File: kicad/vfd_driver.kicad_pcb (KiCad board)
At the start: 2 copper layers, 181.6 x 35.3 mm, 48 parts, among them CON1 AVR-ISP-6, J1 PWR, J2 Display, J6 MH, J7 MH, J8 MH, J9 MH, U1 ATTINY2313-20SU, U10 74HC595, U11 74HC595, U12 74HC595, U13 74HC595, U14 ULN2803A, U15 ULN2803A, U16 ULN2003, U17 ULN2003, U18 LM1117-3.3, U19 LT1073, U2 74HC595, U3 74HC595, U4 74HC595, U5 74HC595, U6 ULN2803A, U7 ULN2003, U8 ULN2003, U9 ULN2003

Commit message: routing
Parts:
- removed J8, J9: MH, Mounting_Holes:MountingHole_3.2mm_M3_DIN965_Pad
- removed U1: ATTINY2313-20SU, Housings_SOIC:SOIC-20W_7.5x12.8mm_Pitch1.27mm
- removed U2, U3, U4: 74HC595, Housings_SOIC:SOIC-16_3.9x9.9mm_Pitch1.27mm
- added J3: MH, Mounting_Holes:MountingHole_3.2mm_M3_DIN965_Pad, F.Cu at (19.1, 49.5)
- added J4: MH, Mounting_Holes:MountingHole_3.2mm_M3_DIN965_Pad, F.Cu at (19.1, 17.8)
- added J5: MH, Mounting_Holes:MountingHole_3.2mm_M3_DIN965_Pad, F.Cu at (191.8, 17.8)
- added R16: 1k, Resistors_SMD:R_0805_HandSoldering, B.Cu at (55.4, 16.8)
- added R17: 1k, Resistors_SMD:R_0805_HandSoldering, B.Cu at (57.4, 16.8)
- added R18: 1k, Resistors_SMD:R_0805_HandSoldering, B.Cu at (59.4, 16.8)
- added R19: 1k, Resistors_SMD:R_0805_HandSoldering, B.Cu at (61.5, 16.8)
- added R20: 1k, Resistors_SMD:R_0805_HandSoldering, B.Cu at (63.5, 16.8)
- added R21: 1k, Resistors_SMD:R_0805_HandSoldering, B.Cu at (65.5, 16.8)
- added R22: 1k, Resistors_SMD:R_0805_HandSoldering, B.Cu at (67.6, 16.8)
- added R23: 1k, Resistors_SMD:R_0805_HandSoldering, B.Cu at (69.6, 16.8)
- added R24: 1k, Resistors_SMD:R_0805_HandSoldering, B.Cu at (71.6, 16.8)
- added R25: 1k, Resistors_SMD:R_0805_HandSoldering, B.Cu at (73.7, 16.8)
- added R26: 1k, Resistors_SMD:R_0805_HandSoldering, B.Cu at (75.7, 16.8)
- added R27: 1k, Resistors_SMD:R_0805_HandSoldering, B.Cu at (77.7, 16.8)
- added R28: 1k, Resistors_SMD:R_0805_HandSoldering, B.Cu at (79.8, 16.8)
- added R29: 1k, Resistors_SMD:R_0805_HandSoldering, B.Cu at (81.8, 16.8)
- added R30: 1k, Resistors_SMD:R_0805_HandSoldering, B.Cu at (83.8, 16.8)
- added R31: 1k, Resistors_SMD:R_0805_HandSoldering, B.Cu at (85.9, 16.8)
- added R32: 1k, Resistors_SMD:R_0805_HandSoldering, B.Cu at (87.9, 16.8)
- added R33: 1k, Resistors_SMD:R_0805_HandSoldering, B.Cu at (89.9, 16.8)
- added R34: 1k, Resistors_SMD:R_0805_HandSoldering, B.Cu at (91.9, 16.8)
- added R35: 1k, Resistors_SMD:R_0805_HandSoldering, B.Cu at (94.0, 16.8)
- added R36: 1k, Resistors_SMD:R_0805_HandSoldering, B.Cu at (96.0, 16.8)
- added R37: 1k, Resistors_SMD:R_0805_HandSoldering, B.Cu at (98.0, 16.8)
- added R38: 1k, Resistors_SMD:R_0805_HandSoldering, B.Cu at (100.1, 16.8)
- added R39: 1k, Resistors_SMD:R_0805_HandSoldering, B.Cu at (102.1, 16.8)
- added R40: 1k, Resistors_SMD:R_0805_HandSoldering, B.Cu at (104.1, 16.8)
- added R41: 1k, Resistors_SMD:R_0805_HandSoldering, B.Cu at (106.2, 16.8)
- added R42: 1k, Resistors_SMD:R_0805_HandSoldering, B.Cu at (108.2, 16.8)
- added R43: 1k, Resistors_SMD:R_0805_HandSoldering, B.Cu at (110.2, 16.8)
- added R44: 1k, Resistors_SMD:R_0805_HandSoldering, B.Cu at (112.3, 16.8)
- added R45: 1k, Resistors_SMD:R_0805_HandSoldering, B.Cu at (114.3, 16.8)
- added R46: 1k, Resistors_SMD:R_0805_HandSoldering, B.Cu at (116.3, 16.8)
- added R47: 1k, Resistors_SMD:R_0805_HandSoldering, B.Cu at (118.4, 16.8)
- added R48: 1k, Resistors_SMD:R_0805_HandSoldering, B.Cu at (120.4, 16.8)
- added R49: 1k, Resistors_SMD:R_0805_HandSoldering, B.Cu at (122.4, 16.8)
- added R50: 1k, Resistors_SMD:R_0805_HandSoldering, B.Cu at (124.5, 16.8)
- added R51: 1k, Resistors_SMD:R_0805_HandSoldering, B.Cu at (126.5, 16.8)
- added R52: 1k, Resistors_SMD:R_0805_HandSoldering, B.Cu at (128.5, 16.8)
- added R53: 1k, Resistors_SMD:R_0805_HandSoldering, B.Cu at (130.6, 16.8)
- added R54: 1k, Resistors_SMD:R_0805_HandSoldering, B.Cu at (132.6, 16.8)
- added R55: 1k, Resistors_SMD:R_0805_HandSoldering, B.Cu at (134.6, 16.8)
- added R56: 1k, Resistors_SMD:R_0805_HandSoldering, B.Cu at (136.7, 16.8)
- added R57: 1k, Resistors_SMD:R_0805_HandSoldering, B.Cu at (138.7, 16.8)
- added R58: 1k, Resistors_SMD:R_0805_HandSoldering, B.Cu at (140.7, 16.8)
- added R59: 1k, Resistors_SMD:R_0805_HandSoldering, B.Cu at (142.7, 16.8)
- added R6: 1M, Resistors_SMD:R_1206, B.Cu at (183.6, 40.4)
- added R60: 1k, Resistors_SMD:R_0805_HandSoldering, B.Cu at (144.8, 16.8)
- added R61: 1k, Resistors_SMD:R_0805_HandSoldering, B.Cu at (146.8, 16.8)
- added R62: 1k, Resistors_SMD:R_0805_HandSoldering, B.Cu at (148.8, 16.8)
- added R63: 1k, Resistors_SMD:R_0805_HandSoldering, B.Cu at (150.9, 16.8)
- added R64: 1k, Resistors_SMD:R_0805_HandSoldering, B.Cu at (152.9, 16.8)
- added R65: 1k, Resistors_SMD:R_0805_HandSoldering, B.Cu at (154.9, 16.8)
- added R66: 1k, Resistors_SMD:R_0805_HandSoldering, B.Cu at (157.0, 16.8)
- added R67: 1k, Resistors_SMD:R_0805_HandSoldering, B.Cu at (159.0, 16.8)
- added R68: 1k, Resistors_SMD:R_0805_HandSoldering, B.Cu at (161.0, 16.8)
- added R69: 1k, Resistors_SMD:R_0805_HandSoldering, B.Cu at (163.1, 16.8)
- added R7: 4k7, Resistors_SMD:R_1206, B.Cu at (183.6, 34.8)
- added R70: 1k, Resistors_SMD:R_0805_HandSoldering, B.Cu at (165.1, 16.8)
- added R71: 1k, Resistors_SMD:R_0805_HandSoldering, B.Cu at (167.1, 16.8)
- added R72: 1k, Resistors_SMD:R_0805_HandSoldering, B.Cu at (169.2, 16.8)
- added R73: 0, Resistors_SMD:R_1206, B.Cu at (65.5, 29.3)
- added R74: 0, Resistors_SMD:R_1206, B.Cu at (78.9, 29.3)
- added R75: 0, Resistors_SMD:R_1206, B.Cu at (93.1, 29.3)
- added R76: 0, Resistors_SMD:R_1206, B.Cu at (106.7, 29.3)
- added R77: 0, Resistors_SMD:R_1206, B.Cu at (120.9, 29.3)
- added R78: 0, Resistors_SMD:R_1206, B.Cu at (136.0, 30.2)
- added R79: 0, Resistors_SMD:R_1206, B.Cu at (152.0, 30.4)
- added R80: 0, Resistors_SMD:R_1206, B.Cu at (146.1, 50.4)
- added U20: 74HC595, Housings_SOIC:SOIC-16_3.9x9.9mm_Pitch1.27mm, B.Cu at (145.4, 43.2)
- added U21: ULN2803A, Housings_SOIC:SOIC-18W_7.5x11.6mm_Pitch1.27mm, B.Cu at (143.5, 30.5)
- added U22: 74HC595, Housings_SOIC:SOIC-16_3.9x9.9mm_Pitch1.27mm, B.Cu at (161.3, 43.2)
- added U23: ULN2803A, Housings_SOIC:SOIC-18W_7.5x11.6mm_Pitch1.27mm, B.Cu at (159.4, 30.5)
- C2: value 100n -> 47µ; footprint Capacitors_SMD:C_0805_HandSoldering -> Capacitors_THT:CP_Radial_Tantal_D4.5mm_P2.50mm
- C4: value 47µ -> 100n; footprint Capacitors_THT:CP_Radial_Tantal_D4.5mm_P2.50mm -> Capacitors_SMD:C_0805_HandSoldering; moved to B.Cu
- D1: value 1N5818 -> LED; footprint Diodes_SMD:D_SMA_Handsoldering -> LEDs:LED_0805
- D2: value LED -> 1N5818; footprint LEDs:LED_0805 -> Diodes_SMD:D_SMA_Handsoldering
- J2: value Display -> MH; footprint modules:vfd_FUTABA_24-SD-01GK_24x1 -> Mounting_Holes:MountingHole_3.2mm_M3_DIN965_Pad
- J6: value MH -> Display; footprint Mounting_Holes:MountingHole_3.2mm_M3_DIN965_Pad -> modules:vfd_FUTABA_24-SD-01GK_24x1
- J7: value MH -> Step; footprint Mounting_Holes:MountingHole_3.2mm_M3_DIN965_Pad -> Connectors:PINHEAD1-2
- R1: value 10k -> 1k; footprint Resistors_SMD:R_1206 -> Capacitors_SMD:C_0805_HandSoldering
- R2: value 100 -> 1k; footprint Resistors_SMD:R_1206 -> Capacitors_SMD:C_0805_HandSoldering
- R3: value 1M -> 10k
- R4: value 4k7 -> 470
- R5: value 470 -> 100
- U11, U13: value 74HC595 -> ULN2003
- U14: value ULN2803A -> 74HC595; footprint Housings_SOIC:SOIC-18W_7.5x11.6mm_Pitch1.27mm -> Housings_SOIC:SOIC-16_3.9x9.9mm_Pitch1.27mm
- U15: value ULN2803A -> ULN2003; footprint Housings_SOIC:SOIC-18W_7.5x11.6mm_Pitch1.27mm -> Housings_SOIC:SOIC-16_3.9x9.9mm_Pitch1.27mm
- U16, U8: value ULN2003 -> 74HC595
- U18: value LM1117-3.3 -> 74HC595; footprint modules:SOT-223_pin4_3 -> Housings_SOIC:SOIC-16_3.9x9.9mm_Pitch1.27mm
- U19: value LT1073 -> ULN2803A; footprint Housings_SOIC:SOIC-8_3.9x4.9mm_Pitch1.27mm -> Housings_SOIC:SOIC-18W_7.5x11.6mm_Pitch1.27mm
- U5: value 74HC595 -> LM1117-3.3; footprint Housings_SOIC:SOIC-16_3.9x9.9mm_Pitch1.27mm -> modules:SOT-223_pin4_3
- U6: value ULN2803A -> ATTINY2313-20SU; footprint Housings_SOIC:SOIC-18W_7.5x11.6mm_Pitch1.27mm -> Housings_SOIC:SOIC-20W_7.5x12.8mm_Pitch1.27mm
- U7: value ULN2003 -> LT1073; footprint Housings_SOIC:SOIC-16_3.9x9.9mm_Pitch1.27mm -> Housings_SOIC:SOIC-8_3.9x4.9mm_Pitch1.27mm
- moved R4 152.9 mm to (38.5, 49.9), turned to 270 degrees
- moved D2 151.8 mm to (177.3, 40.9)
- moved R3 148.3 mm to (42.0, 26.5)
- moved R5 147.4 mm to (171.7, 35.8)
- moved D1 138.2 mm to (40.9, 49.9), turned to 270 degrees
- moved R2 131.4 mm to (53.3, 16.8)
- moved U7 118.5 mm to (177.3, 35.1), turned to 0 degrees
- moved R13 109.0 mm to (52.2, 48.4), turned to 90 degrees
- moved U6 94.8 mm to (36.8, 35.6), turned to 180 degrees
- moved U11 92.4 mm to (72.1, 27.9), turned to 90 degrees
- moved J6 90.7 mm to (110.4, 20.7), turned to 90 degrees
- moved U18 90.3 mm to (130.2, 43.2), turned to 270 degrees
- moved J2 85.3 mm to (191.8, 49.5)
- moved R8 80.4 mm to (49.1, 48.4)
- moved U10 74.7 mm to (73.4, 38.7)
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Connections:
- C2 pad 1: GND -> Net-(C2-Pad1)
- C2 pad 2: VCC -> GND
- C3 pad 1: Net-(C3-Pad1) -> VCC
- C4 pad 1: VCC -> GND
- C4 pad 2: GND -> VCC
- D1 pad 1: +36V -> GND
- D2 pad 1: GND -> +36V
- J1 pad 2: Net-(C3-Pad1) -> Net-(C2-Pad1)
- J6 pad 1: GND -> VCC
- L1 pad 1: VCC -> Net-(J7-Pad2)
- L1 pad 2: Net-(D1-Pad2) -> Net-(D2-Pad2)
- R1 pad 1: VCC -> +36V
- R1 pad 2: /reset -> /Sheet59FF2CCC/L1_1
- R10 pad 1: Net-(R10-Pad1) -> /Sheet5A12BB8F/RCLK
- R10 pad 2: /SER -> /Sheet5A11F95F/RCLK
- R11 pad 1: Net-(R11-Pad1) -> /Sheet5A11F95F/RCLK
- R11 pad 2: /SER -> /Sheet5A12BB9F/RCLK
- R12 pad 1: Net-(R12-Pad1) -> /Sheet5A12BB9F/RCLK
- R12 pad 2: /SER -> /Sheet5A12BBAF/RCLK
- R13 pad 2: /SER -> /SER_POS
- R14 pad 1: Net-(R14-Pad1) -> /Sheet5A13BBCF/SER
- R14 pad 2: /SER -> /Sheet5A13BBAF/SER_OUT
- R15 pad 1: Net-(R15-Pad1) -> /Sheet5A13BBBF/SER
- R15 pad 2: /SER -> /Sheet5A13BBCF/SER_OUT
- R2 pad 1: VCC -> +36V
- R2 pad 2: Net-(R2-Pad2) -> /Sheet59FF2CCC/L1_2
- R3 pad 1: +36V -> VCC
- R3 pad 2: Net-(R3-Pad2) -> /reset
- R4 pad 1: Net-(R3-Pad2) -> VCC
- R4 pad 2: GND -> Net-(D1-Pad2)
- R5 pad 1: VCC -> Net-(J7-Pad2)
- R5 pad 2: Net-(D2-Pad2) -> Net-(R5-Pad2)
- R8 pad 1: Net-(R8-Pad1) -> /RCLK_0
- R8 pad 2: /SER -> /Sheet5A13BBAF/RCLK
- R9 pad 1: Net-(R9-Pad1) -> /RCLK_7
- R9 pad 2: /SER -> /Sheet5A12BB8F/RCLK
- U10 pad 10: /SRCLR -> Net-(R74-Pad1)
- U10 pad 12: /RCLK_1 -> /Sheet5A12BB8F/RCLK
- U10 pad 14: Net-(R12-Pad1) -> /Sheet5A12BB8F/SER
- U10 pad 15: Net-(U10-Pad15) -> (no net)
- U10 pad 9: (no net) -> /Sheet5A11F95F/SER
- U11 pad 1: Net-(U11-Pad1) -> Net-(U10-Pad7)
- U11 pad 10: /SRCLR -> /Sheet59FF2CCC/L2_1
- U11 pad 11: /SRCLK -> /Sheet59FF2CCC/L2_2
- U11 pad 12: /RCLK_2 -> /Sheet59FF2CCC/L2_3
- U11 pad 13: GND -> /Sheet59FF2CCC/L2_4
- U11 pad 14: Net-(R13-Pad1) -> /Sheet59FF2CCC/L2_5
- U11 pad 15: Net-(U11-Pad15) -> /Sheet59FF2CCC/L2_6
- U11 pad 16: VCC -> /Sheet59FF2CCC/L2_7
- U11 pad 2: Net-(U11-Pad2) -> Net-(U10-Pad6)
- U11 pad 3: Net-(U11-Pad3) -> Net-(U10-Pad5)
- U11 pad 4: Net-(U11-Pad4) -> Net-(U10-Pad4)
- U11 pad 5: Net-(U11-Pad5) -> Net-(U10-Pad3)
- U11 pad 6: Net-(U11-Pad6) -> Net-(U10-Pad2)
- U11 pad 7: Net-(U11-Pad7) -> Net-(U10-Pad1)
- U11 pad 9: (no net) -> +36V
- U12 pad 10: /SRCLR -> Net-(R75-Pad1)
- U12 pad 12: /RCLK_5 -> /Sheet5A11F95F/RCLK
- U12 pad 14: Net-(R14-Pad1) -> /Sheet5A11F95F/SER
- U12 pad 9: (no net) -> /Sheet5A12BB9F/SER
- U13 pad 1: Net-(U13-Pad1) -> Net-(U12-Pad7)
- U13 pad 10: /SRCLR -> /Sheet59FF2CCC/L3_1
- U13 pad 11: /SRCLK -> /Sheet59FF2CCC/L3_2
- U13 pad 12: /RCLK_7 -> /Sheet59FF2CCC/L3_3
- U13 pad 13: GND -> /Sheet59FF2CCC/L3_4
- U13 pad 14: Net-(R15-Pad1) -> /Sheet59FF2CCC/L3_5
- U13 pad 15: (no net) -> /Sheet59FF2CCC/L3_6
- U13 pad 16: VCC -> /Sheet59FF2CCC/L3_7
- U13 pad 2: Net-(U13-Pad2) -> Net-(U12-Pad6)
- U13 pad 3: Net-(U13-Pad3) -> Net-(U12-Pad5)
- U13 pad 4: Net-(U13-Pad4) -> Net-(U12-Pad4)
- U13 pad 5: Net-(U13-Pad5) -> Net-(U12-Pad3)
- U13 pad 6: Net-(U13-Pad6) -> Net-(U12-Pad2)
- U13 pad 7: Net-(U13-Pad7) -> Net-(U12-Pad1)
- U13 pad 9: (no net) -> +36V
- U14 pad 1: Net-(U10-Pad7) -> Net-(U14-Pad1)
- U14 pad 10: +36V -> Net-(R76-Pad1)
- U14 pad 11: /G21 -> /SRCLK
- U14 pad 12: /G22 -> /Sheet5A12BB9F/RCLK
- U14 pad 13: /G23 -> GND
- U14 pad 14: /G24 -> /Sheet5A12BB9F/SER
- U14 pad 15: /G25 -> (no net)
- U14 pad 16: /G26 -> VCC
- U14 pad 2: Net-(U10-Pad6) -> Net-(U14-Pad2)
- U14 pad 3: Net-(U10-Pad5) -> Net-(U14-Pad3)
- U14 pad 4: Net-(U10-Pad4) -> Net-(U14-Pad4)
- U14 pad 5: Net-(U10-Pad3) -> Net-(U14-Pad5)
- U14 pad 6: Net-(U10-Pad2) -> Net-(U14-Pad6)
- U14 pad 7: Net-(U10-Pad1) -> Net-(U14-Pad7)
- U14 pad 8: Net-(U10-Pad15) -> GND
- U14 pad 9: GND -> /Sheet5A12BBAF/SER
- U15 pad 1: Net-(U11-Pad7) -> Net-(U14-Pad7)
- U15 pad 10: +36V -> /Sheet59FF2CCC/L4_1
- U15 pad 11: /G31 -> /Sheet59FF2CCC/L4_2
- U15 pad 12: /G32 -> /Sheet59FF2CCC/L4_3
- U15 pad 13: /G33 -> /Sheet59FF2CCC/L4_4
- U15 pad 14: /G34 -> /Sheet59FF2CCC/L4_5
- U15 pad 15: /G35 -> /Sheet59FF2CCC/L4_6
- U15 pad 16: /G36 -> /Sheet59FF2CCC/L4_7
- U15 pad 2: Net-(U11-Pad6) -> Net-(U14-Pad6)
- U15 pad 3: Net-(U11-Pad5) -> Net-(U14-Pad5)
- U15 pad 4: Net-(U11-Pad4) -> Net-(U14-Pad4)
- U15 pad 5: Net-(U11-Pad3) -> Net-(U14-Pad3)
- U15 pad 6: Net-(U11-Pad2) -> Net-(U14-Pad2)
- U15 pad 7: Net-(U11-Pad1) -> Net-(U14-Pad1)
- U15 pad 8: Net-(U11-Pad15) -> GND
- U15 pad 9: GND -> +36V
- U16 pad 1: Net-(U12-Pad7) -> Net-(U16-Pad1)
- U16 pad 10: /L31 -> Net-(R77-Pad1)
- U16 pad 11: /L32 -> /SRCLK
- U16 pad 12: /L33 -> /Sheet5A12BBAF/RCLK
- U16 pad 13: /L34 -> GND
- U16 pad 14: /L35 -> /Sheet5A12BBAF/SER
- U16 pad 15: /L36 -> (no net)
- U16 pad 16: /L37 -> VCC
- U16 pad 2: Net-(U12-Pad6) -> Net-(U16-Pad2)
- U16 pad 3: Net-(U12-Pad5) -> Net-(U16-Pad3)
- U16 pad 4: Net-(U12-Pad4) -> Net-(U16-Pad4)
- U16 pad 5: Net-(U12-Pad3) -> Net-(U16-Pad5)
- U16 pad 6: Net-(U12-Pad2) -> Net-(U16-Pad6)
- U16 pad 7: Net-(U12-Pad1) -> Net-(U16-Pad7)
- U16 pad 9: +36V -> (no net)
- U17 pad 1: Net-(U13-Pad7) -> Net-(U16-Pad7)
- U17 pad 10: /L51 -> /Sheet59FF2CCC/L5_1
- U17 pad 11: /L52 -> /Sheet59FF2CCC/L5_2
- U17 pad 12: /L53 -> /Sheet59FF2CCC/L5_3
- U17 pad 13: /L54 -> /Sheet59FF2CCC/L5_4
- U17 pad 14: /L55 -> /Sheet59FF2CCC/L5_5
- U17 pad 15: /L56 -> /Sheet59FF2CCC/L5_6
- U17 pad 16: /L57 -> /Sheet59FF2CCC/L5_7
- U17 pad 2: Net-(U13-Pad6) -> Net-(U16-Pad6)
- U17 pad 3: Net-(U13-Pad5) -> Net-(U16-Pad5)
- U17 pad 4: Net-(U13-Pad4) -> Net-(U16-Pad4)
- U17 pad 5: Net-(U13-Pad3) -> Net-(U16-Pad3)
- U17 pad 6: Net-(U13-Pad2) -> Net-(U16-Pad2)
- U17 pad 7: Net-(U13-Pad1) -> Net-(U16-Pad1)
- U18 pad 1: GND -> Net-(U18-Pad1)
- U18 pad 2: VCC -> Net-(U18-Pad2)
- U18 pad 3: Net-(C3-Pad1) -> Net-(U18-Pad3)
- U19 pad 1: Net-(R2-Pad2) -> Net-(U18-Pad7)
- U19 pad 2: VCC -> Net-(U18-Pad6)
- U19 pad 3: Net-(D1-Pad2) -> Net-(U18-Pad5)
- U19 pad 4: GND -> Net-(U18-Pad4)
- U19 pad 5: GND -> Net-(U18-Pad3)
- U19 pad 6: (no net) -> Net-(U18-Pad2)
- U19 pad 7: (no net) -> Net-(U18-Pad1)
- U19 pad 8: Net-(R3-Pad2) -> Net-(U18-Pad15)
- U5 pad 1: Net-(U5-Pad1) -> GND
- U5 pad 2: Net-(U5-Pad2) -> VCC
- U5 pad 3: Net-(U5-Pad3) -> Net-(C2-Pad1)
- U6 pad 1: Net-(U2-Pad7) -> /reset
- U6 pad 10: +36V -> GND
- U6 pad 11: /G11 -> (no net)
- U6 pad 12: /G12 -> (no net)
- U6 pad 13: /G13 -> (no net)
- U6 pad 14: /G14 -> (no net)
- U6 pad 15: /G15 -> (no net)
- U6 pad 16: /G16 -> (no net)
- U6 pad 17: /G17 -> /MOSI
- U6 pad 18: /G18 -> /MISO
- U6 pad 2: Net-(U2-Pad6) -> /SRCLR
- U6 pad 3: Net-(U2-Pad5) -> /SRCLK
- U6 pad 4: Net-(U2-Pad4) -> (no net)
- U6 pad 5: Net-(U2-Pad3) -> /RCLK_7
- U6 pad 6: Net-(U2-Pad2) -> /SER_DAT
- U6 pad 7: Net-(U2-Pad1) -> /SER_POS
- U6 pad 8: Net-(U2-Pad15) -> /RCLK_0
- U6 pad 9: GND -> (no net)
- U7 pad 1: Net-(U3-Pad7) -> Net-(R5-Pad2)
- U7 pad 2: Net-(U3-Pad6) -> Net-(J7-Pad2)
- U7 pad 3: Net-(U3-Pad5) -> Net-(D2-Pad2)
- U7 pad 4: Net-(U3-Pad4) -> GND
- U7 pad 5: Net-(U3-Pad3) -> GND
- U7 pad 6: Net-(U3-Pad2) -> (no net)
- U7 pad 7: Net-(U3-Pad1) -> (no net)
- U7 pad 8: GND -> Net-(R6-Pad2)
- U8 pad 1: Net-(U4-Pad7) -> Net-(U8-Pad1)
- U8 pad 10: /L21 -> Net-(R73-Pad1)
- U8 pad 11: /L22 -> /SRCLK
- U8 pad 12: /L23 -> /RCLK_7
- U8 pad 13: /L24 -> GND
- U8 pad 14: /L25 -> /SER_DAT
- U8 pad 15: /L26 -> (no net)
- U8 pad 16: /L27 -> VCC
- U8 pad 2: Net-(U4-Pad6) -> Net-(U8-Pad2)
- U8 pad 3: Net-(U4-Pad5) -> Net-(U8-Pad3)
- U8 pad 4: Net-(U4-Pad4) -> Net-(U8-Pad4)
- U8 pad 5: Net-(U4-Pad3) -> Net-(U8-Pad5)
- U8 pad 6: Net-(U4-Pad2) -> Net-(U8-Pad6)
- U8 pad 7: Net-(U4-Pad1) -> Net-(U8-Pad7)
- U8 pad 9: +36V -> /Sheet5A12BB8F/SER
- U9 pad 1: Net-(U5-Pad7) -> Net-(U8-Pad7)
- U9 pad 10: /L47 -> /Sheet59FF2CCC/L1_1
- U9 pad 11: /L46 -> /Sheet59FF2CCC/L1_2
- U9 pad 12: /L45 -> /Sheet59FF2CCC/L1_3
- U9 pad 13: /L44 -> /Sheet59FF2CCC/L1_4
- U9 pad 14: /L43 -> /Sheet59FF2CCC/L1_5
- U9 pad 15: /L42 -> /Sheet59FF2CCC/L1_6
- U9 pad 16: /L41 -> /Sheet59FF2CCC/L1_7
- U9 pad 2: Net-(U5-Pad6) -> Net-(U8-Pad6)
- U9 pad 3: Net-(U5-Pad5) -> Net-(U8-Pad5)
- U9 pad 4: Net-(U5-Pad4) -> Net-(U8-Pad4)
- U9 pad 5: Net-(U5-Pad3) -> Net-(U8-Pad3)
- U9 pad 6: Net-(U5-Pad2) -> Net-(U8-Pad2)
- U9 pad 7: Net-(U5-Pad1) -> Net-(U8-Pad1)
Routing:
- net GND: track 263.7 -> 11.2 mm, vias 18 -> 0
- net +36V: track 161.6 -> 347.3 mm
- net /RCLK_2: track 151.9 -> 0.00 mm
- net /SER: track 150.3 -> 0.00 mm
- net /RCLK_1: track 135.1 -> 0.00 mm
- net /Sheet5A13BBAF/RCLK: track 0.00 -> 124.2 mm
- net /RCLK_0: track 120.5 -> 12.1 mm
- net Net-(R13-Pad1): track 2.94 -> 80.0 mm
- net /RCLK_6: track 69.5 -> 0.00 mm
- net /RCLK_7: track 102.1 -> 32.6 mm
- net /SRCLK: track 199.8 -> 267.1 mm
- net VCC: track 309.4 -> 250.1 mm, vias 21 -> 4
- net /RCLK_5: track 52.7 -> 0.00 mm
- net Net-(J7-Pad2): track 0.00 -> 47.8 mm
- net Net-(D1-Pad2): track 43.6 -> 2.56 mm
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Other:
- board size 181.6 x 35.3 mm -> 181.6 x 40.6 mm

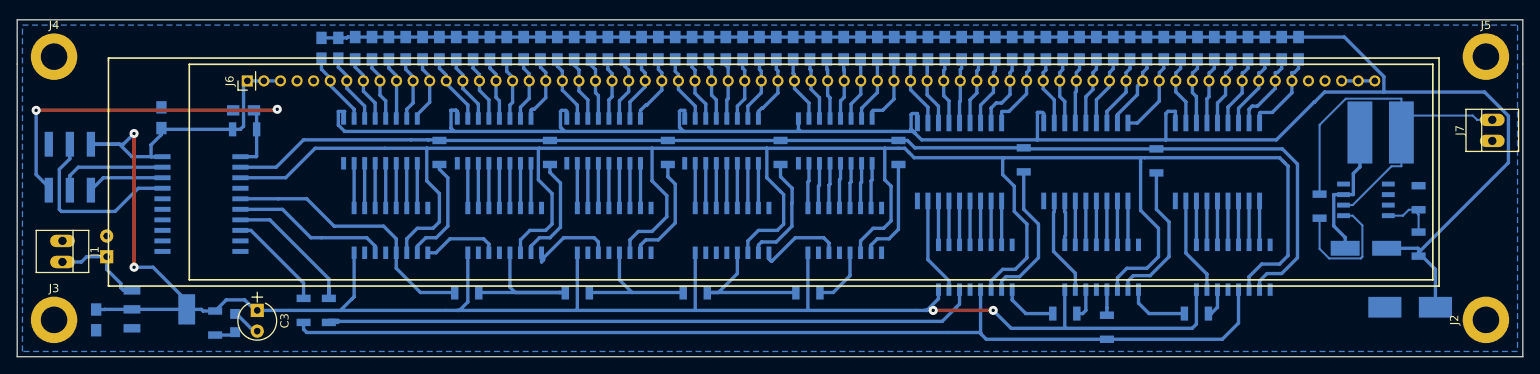
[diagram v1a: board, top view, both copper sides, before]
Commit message: Not working need high side driver
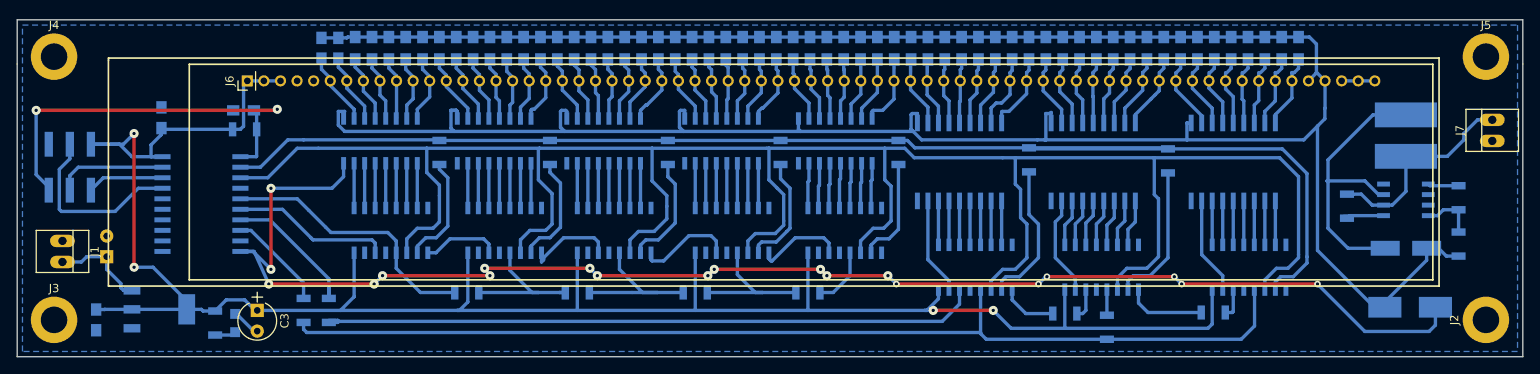
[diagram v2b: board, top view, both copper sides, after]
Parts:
- moved D2 4.83 mm to (182.1, 40.9)
- moved R6 4.83 mm to (188.5, 40.4)
- moved R7 4.83 mm to (188.5, 34.8)
- moved U7 4.83 mm to (182.1, 35.1)
- moved R5 3.30 mm to (175.0, 35.8)
- moved L1 3.07 mm to (182.1, 27.3), turned to 90 degrees
- moved R15 2.04 mm to (158.9, 48.6)
- moved U22 1.91 mm to (163.2, 43.2)
- moved U23 1.91 mm to (161.3, 30.5)
- moved R79 1.40 mm to (153.4, 30.4)
- moved U21 0.89 mm to (144.4, 30.5)
- moved R78 0.63 mm to (136.7, 30.2)
- turned C6 to 0 degrees
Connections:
- J6 pad 65: (no net) -> +36V
- J6 pad 66: (no net) -> +36V
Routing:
- net GND: track 11.2 -> 196.1 mm, vias 0 -> 20
- net +36V: track 347.3 -> 324.9 mm
- net Net-(J7-Pad2): track 47.8 -> 26.4 mm
- net Net-(D2-Pad2): track 17.2 -> 35.5 mm
- net /SRCLR: track 148.0 -> 165.5 mm
- net /Sheet5A12BB9F/SER: track 0.00 -> 11.7 mm
- net Net-(R5-Pad2): track 16.0 -> 5.64 mm
- net /Sheet5A12BB8F/RCLK: track 21.5 -> 17.4 mm
- net /Sheet5A11F95F/RCLK: track 16.7 -> 19.1 mm
- net /Sheet5A13BBAF/RCLK: track 124.2 -> 126.4 mm
- net /Sheet5A13BBCF/SER_OUT: track 7.68 -> 9.66 mm
- net /SRCLK: track 267.1 -> 265.5 mm
- net /Sheet59FF2CCC/G3_8: track 10.6 -> 8.99 mm
- net VCC: track 250.1 -> 251.5 mm
- net /Sheet59FF2CCC/G3_7: track 9.82 -> 8.66 mm
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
